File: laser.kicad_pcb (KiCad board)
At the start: 2 copper layers, 90.2 x 50.9 mm, 127 parts, among them IC201 ADM7172ACPZ-4.2-R7, IC202 LT1716CS5#TRPBF, IC203 ADM7154ARDZ-3.3-R7, IC204 IRF9358PBF, IC601 ATMEGA328P-AU, IC602 FT232RL-TUBE, IC701 MAX6126AASA25+, IC801 ADS122C04IPWR, J601 M20-9980345, J602 USB_Connector, Q401 RSR030N06TL, U101 281698-3, U201 LM4040EIM3X-2.5_NOPB, U301 OPA569AIDWPR, U302 OPA569AIDWPR, U401 ADA4528-2ACPZ-RL, U402 782853152_WE-CBA_08, U501 ADA4528-2ACPZ-RL, U502 ADA4528-2ACPZ-RL, U801 MAX5217GUA+, U802 MAX5217GUA+, Y601 ECS-160-16-33B-CKM-TR

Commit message: SOLVED: GND and 4.2V
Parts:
- moved C606 11.9 mm to (199.7, 101.5), turned to 90 degrees
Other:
- copper layers 2 -> 4
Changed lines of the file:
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@@
   (layers
     (0 F.Cu signal)
+    (1 GND power)
+    (2 PWR power)
     (31 B.Cu signal)
     (32 B.Adhes user)
@@
   )
   (module Capacitor_SMD:C_0402_1005Metric (layer F.Cu)
-    (at 200.09 89.61)
-    (descr "Capacitor SMD 0402 (1005 Metric), square (rectangular) end terminal, IPC_7351 nominal, (Body size source: IPC-SM-782 page 76, https://www.pcb-3d.com/wordpress/wp-content/uploads/ipc-sm-782a_amendment_1_and_2.pdf), generated with kicad-footprint-generator")
-    (tags capacitor)
-    (attr smd)
-    (fp_text reference C606 (at 0 -1.16) (layer F.SilkS)
-      (effects (font (size 1 1) (thickness 0.15)))
-    )
-    (fp_text value 100nF (at 0 1.16) (layer F.Fab)
-      (effects (font (size 1 1) (thickness 0.15)))
-    )
-    (fp_line (start -0.5 0.25) (end -0.5 -0.25) (layer F.Fab) (width 0.1))
-    (fp_line (start -0.5 -0.25) (end 0.5 -0.25) (layer F.Fab) (width 0.1))
-    (fp_line (start 0.5 -0.25) (end 0.5 0.25) (layer F.Fab) (width 0.1))
-    (fp_line (start 0.5 0.25) (end -0.5 0.25) (layer F.Fab) (width 0.1))
-    (fp_line (start -0.107836 -0.36) (end 0.107836 -0.36) (layer F.SilkS) (width 0.12))
-    (fp_line (start -0.107836 0.36) (end 0.107836 0.36) (layer F.SilkS) (width 0.12))
-    (fp_line (start -0.91 0.46) (end -0.91 -0.46) (layer F.CrtYd) (width 0.05))
-    (fp_line (start -0.91 -0.46) (end 0.91 -0.46) (layer F.CrtYd) (width 0.05))
-    (fp_line (start 0.91 -0.46) (end 0.91 0.46) (layer F.CrtYd) (width 0.05))
-    (fp_line (start 0.91 0.46) (end -0.91 0.46) (layer F.CrtYd) (width 0.05))
-    (fp_text user %R (at 0 0) (layer F.Fab)
-      (effects (font (size 0.25 0.25) (thickness 0.04)))
-    )
-    (pad 1 smd roundrect (at -0.48 0) (size 0.56 0.62) (layers F.Cu F.Paste F.Mask) (roundrect_rratio 0.25)
+    (at 199.73 101.53 90)
+    (descr "Capacitor SMD 0402 (1005 Metric), square (rectangular) end terminal, IPC_7351 nominal, (Body size source: IPC-SM-782 page 76, https://www.pcb-3d.com/wordpress/wp-content/uploads/ipc-sm-782a_amendment_1_and_2.pdf), generated with kicad-footprint-generator")
+    (tags capacitor)
+    (attr smd)
+    (fp_text reference C606 (at 0 -1.16 90) (layer F.SilkS)
+      (effects (font (size 1 1) (thickness 0.15)))
+    )
+    (fp_text value 100nF (at 0 1.16 90) (layer F.Fab)
+      (effects (font (size 1 1) (thickness 0.15)))
+    )
+    (fp_line (start -0.5 0.25) (end -0.5 -0.25) (layer F.Fab) (width 0.1))
+    (fp_line (start -0.5 -0.25) (end 0.5 -0.25) (layer F.Fab) (width 0.1))
+    (fp_line (start 0.5 -0.25) (end 0.5 0.25) (layer F.Fab) (width 0.1))
+    (fp_line (start 0.5 0.25) (end -0.5 0.25) (layer F.Fab) (width 0.1))
+    (fp_line (start -0.107836 -0.36) (end 0.107836 -0.36) (layer F.SilkS) (width 0.12))
+    (fp_line (start -0.107836 0.36) (end 0.107836 0.36) (layer F.SilkS) (width 0.12))
+    (fp_line (start -0.91 0.46) (end -0.91 -0.46) (layer F.CrtYd) (width 0.05))
+    (fp_line (start -0.91 -0.46) (end 0.91 -0.46) (layer F.CrtYd) (width 0.05))
+    (fp_line (start 0.91 -0.46) (end 0.91 0.46) (layer F.CrtYd) (width 0.05))
+    (fp_line (start 0.91 0.46) (end -0.91 0.46) (layer F.CrtYd) (width 0.05))
+    (fp_text user %R (at 0 0 90) (layer F.Fab)
+      (effects (font (size 0.25 0.25) (thickness 0.04)))
+    )
+    (pad 1 smd roundrect (at -0.48 0 90) (size 0.56 0.62) (layers F.Cu F.Paste F.Mask) (roundrect_rratio 0.25)
       (net 35 "Net-(C606-Pad1)"))
-    (pad 2 smd roundrect (at 0.48 0) (size 0.56 0.62) (layers F.Cu F.Paste F.Mask) (roundrect_rratio 0.25)
-      (net 2 4.2V))
-    (model ${KISYS3DMOD}/Capacitor_SMD.3dshapes/C_0402_1005Metric.wrl
+    (pad 2 smd roundrect (at 0.48 0 90) (size 0.56 0.62) (layers F.Cu F.Paste F.Mask) (roundrect_rratio 0.25)
+      (net 2 4.2V))
+    (model ${KISYS3DMOD}/Capacitor_SMD.3dshapes/C_0402_1005Metric.wrl

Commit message: final push for any last changes 6/18
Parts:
- added C305: 100u, Capacitor_SMD:C_0402_1005Metric, F.Cu at (165.8, 118.4)
- added C306: 100u, Capacitor_SMD:C_0402_1005Metric, F.Cu at (166.3, 123.2)
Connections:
- B1 pad 2: 4.2V -> Monitor+_To_AIN2
- B1 pad 4: 4.2V -> Monitor+_To_AIN2
- B1 pad 5: 4.2V -> Monitor+_To_AIN2
- B1 pad 8: 4.2V -> Monitor+_To_AIN2
- B1 pad 9: 4.2V -> Monitor+_To_AIN2
- C201 pad 2: 4.2V -> Monitor+_To_AIN2
- C202 pad 2: 4.2V -> Monitor+_To_AIN2
- C203 pad 2: 4.2V -> Monitor+_To_AIN2
- C204 pad 1: 4.2V -> Monitor+_To_AIN2
- C206 pad 1: 4.2V -> Monitor+_To_AIN2
- C207 pad 1: 4.2V -> Monitor+_To_AIN2
- C208 pad 1: 4.2V -> Monitor+_To_AIN2
- C209 pad 2: 4.2V -> Monitor+_To_AIN2
- C210 pad 1: 4.2V -> Monitor+_To_AIN2
- C211 pad 1: 4.2V -> Monitor+_To_AIN2
- C212 pad 2: 4.2V -> Monitor+_To_AIN2
- C302 pad 1: 4.2V -> Monitor+_To_AIN2
- C303 pad 1: 4.2V -> Monitor+_To_AIN2
- C307 pad 2: 4.2V -> Monitor+_To_AIN2
- C308 pad 2: 4.2V -> Monitor+_To_AIN2
- C309 pad 1: 4.2V -> Monitor+_To_AIN2
- C310 pad 1: 4.2V -> Monitor+_To_AIN2
- C311 pad 1: 4.2V -> Monitor+_To_AIN2
- C312 pad 1: 4.2V -> Monitor+_To_AIN2
- C402 pad 1: 4.2V -> Monitor+_To_AIN2
- C403 pad 2: 4.2V -> Monitor+_To_AIN2
- C404 pad 2: 4.2V -> Monitor+_To_AIN2
- C405 pad 2: 4.2V -> Monitor+_To_AIN2
- C406 pad 2: 4.2V -> Monitor+_To_AIN2
- C407 pad 1: 4.2V -> Monitor+_To_AIN2
- C408 pad 2: 4.2V -> Monitor+_To_AIN2
- C501 pad 2: 4.2V -> Monitor+_To_AIN2
- C502 pad 2: 4.2V -> Monitor+_To_AIN2
- C503 pad 2: 4.2V -> Monitor+_To_AIN2
- C504 pad 2: 4.2V -> Monitor+_To_AIN2
- C505 pad 2: 4.2V -> Monitor+_To_AIN2
- C506 pad 2: 4.2V -> Monitor+_To_AIN2
- C507 pad 2: 4.2V -> Monitor+_To_AIN2
- C601 pad 2: 4.2V -> Monitor+_To_AIN2
- C602 pad 2: 4.2V -> Monitor+_To_AIN2
- C603 pad 2: 4.2V -> Monitor+_To_AIN2
- C604 pad 2: 4.2V -> Monitor+_To_AIN2
- C605 pad 2: 4.2V -> Monitor+_To_AIN2
- C606 pad 2: 4.2V -> Monitor+_To_AIN2
- C701 pad 2: 4.2V -> Monitor+_To_AIN2
- C702 pad 2: 4.2V -> Monitor+_To_AIN2
- C703 pad 2: 4.2V -> Monitor+_To_AIN2
- C704 pad 2: 4.2V -> Monitor+_To_AIN2
- C705 pad 2: 4.2V -> Monitor+_To_AIN2
- C801 pad 2: 4.2V -> Monitor+_To_AIN2
- C802 pad 2: 4.2V -> Monitor+_To_AIN2
- C803 pad 2: 4.2V -> Monitor+_To_AIN2
- C804 pad 2: 4.2V -> Monitor+_To_AIN2
- C805 pad 2: 4.2V -> Monitor+_To_AIN2
- C806 pad 2: 4.2V -> Monitor+_To_AIN2
- C807 pad 2: 4.2V -> Monitor+_To_AIN2
- C808 pad 2: 4.2V -> Monitor+_To_AIN2
- C809 pad 2: 4.2V -> Monitor+_To_AIN2
- C810 pad 2: 4.2V -> Monitor+_To_AIN2
- C811 pad 2: 4.2V -> Monitor+_To_AIN2
- IC201 pad 6: 4.2V -> Monitor+_To_AIN2
- IC201 pad 9: 4.2V -> Monitor+_To_AIN2
- IC202 pad 2: 4.2V -> Monitor+_To_AIN2
- IC203 pad 4: 4.2V -> Monitor+_To_AIN2
- IC204 pad 2: 4.2V -> Monitor+_To_AIN2
- IC601 pad 21: 4.2V -> Monitor+_To_AIN2
- IC601 pad 3: 4.2V -> Monitor+_To_AIN2
- IC601 pad 5: 4.2V -> Monitor+_To_AIN2
- IC602 pad 18: 4.2V -> Monitor+_To_AIN2
- IC602 pad 21: 4.2V -> Monitor+_To_AIN2
- IC602 pad 25: 4.2V -> Monitor+_To_AIN2
- IC602 pad 26: 4.2V -> Monitor+_To_AIN2
- IC602 pad 7: 4.2V -> Monitor+_To_AIN2
- IC701 pad 3: 4.2V -> Monitor+_To_AIN2
- IC701 pad 4: 4.2V -> Monitor+_To_AIN2
- IC801 pad 1: 4.2V -> Monitor+_To_AIN2
- IC801 pad 10: 4.2V -> Monitor+_To_AIN2
- IC801 pad 2: 4.2V -> Monitor+_To_AIN2
- IC801 pad 4: 4.2V -> Monitor+_To_AIN2
- IC801 pad 5: 4.2V -> Monitor+_To_AIN2
- IC801 pad 7: 4.2V -> Monitor+_To_AIN2
- IC801 pad 8: 4.2V -> Monitor+_To_AIN2
- J601 pad 6: 4.2V -> Monitor+_To_AIN2
- J602 pad 1: 4.2V -> Monitor+_To_AIN2
- J602 pad 6: 4.2V -> Monitor+_To_AIN2
- J602 pad 7: 4.2V -> Monitor+_To_AIN2
- J602 pad 8: 4.2V -> Monitor+_To_AIN2
- J602 pad 9: 4.2V -> Monitor+_To_AIN2
- R203 pad 2: 4.2V -> Monitor+_To_AIN2
- R302 pad 2: 4.2V -> Monitor+_To_AIN2
- R305 pad 2: 4.2V -> Monitor+_To_AIN2
- R306 pad 2: 4.2V -> Monitor+_To_AIN2
- R308 pad 1: 4.2V -> Monitor+_To_AIN2
- R309 pad 1: 4.2V -> Monitor+_To_AIN2
- R407 pad E1: 4.2V -> Monitor+_To_AIN2
- R407 pad I1: 4.2V -> Monitor+_To_AIN2
- R803 pad 2: 4.2V -> Monitor+_To_AIN2
- R804 pad 2: 4.2V -> Monitor+_To_AIN2
- U101 pad 1: 4.2V -> Monitor+_To_AIN2
- U201 pad 2: 4.2V -> Monitor+_To_AIN2
- U301 pad 1: 4.2V -> Monitor+_To_AIN2
- U301 pad 10: 4.2V -> Monitor+_To_AIN2
- U301 pad 11: 4.2V -> Monitor+_To_AIN2
- U301 pad 13: Net-(C305-Pad2) -> 4.2V
- U301 pad 17: 4.2V -> Monitor+_To_AIN2
- U301 pad 18: 4.2V -> Monitor+_To_AIN2
- U301 pad 20: 4.2V -> Monitor+_To_AIN2
- U302 pad 1: 4.2V -> Monitor+_To_AIN2
- U302 pad 10: 4.2V -> Monitor+_To_AIN2
- U302 pad 11: 4.2V -> Monitor+_To_AIN2
- U302 pad 13: Net-(C306-Pad2) -> 4.2V
- U302 pad 17: 4.2V -> Monitor+_To_AIN2
- U302 pad 18: 4.2V -> Monitor+_To_AIN2
- U302 pad 20: 4.2V -> Monitor+_To_AIN2
- U401 pad 4: 4.2V -> Monitor+_To_AIN2
- U501 pad 4: 4.2V -> Monitor+_To_AIN2
- U502 pad 4: 4.2V -> Monitor+_To_AIN2
- U801 pad 8: 4.2V -> Monitor+_To_AIN2
- U802 pad 2: 4.2V -> Monitor+_To_AIN2
- U802 pad 8: 4.2V -> Monitor+_To_AIN2
- Y601 pad 2: 4.2V -> Monitor+_To_AIN2
- Y601 pad 4: 4.2V -> Monitor+_To_AIN2

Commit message: GND works
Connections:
- B1 pad 2: Monitor+_To_AIN2 -> GND
- B1 pad 5: Monitor+_To_AIN2 -> GND
- B1 pad 8: Monitor+_To_AIN2 -> GND
- B1 pad 9: Monitor+_To_AIN2 -> GND
- C201 pad 2: Monitor+_To_AIN2 -> GND
- C202 pad 2: Monitor+_To_AIN2 -> GND
- C203 pad 2: Monitor+_To_AIN2 -> GND
- C204 pad 1: Monitor+_To_AIN2 -> GND
- C206 pad 1: Monitor+_To_AIN2 -> GND
- C207 pad 1: Monitor+_To_AIN2 -> GND
- C208 pad 1: Monitor+_To_AIN2 -> GND
- C209 pad 2: Monitor+_To_AIN2 -> GND
- C210 pad 1: Monitor+_To_AIN2 -> GND
- C211 pad 1: Monitor+_To_AIN2 -> GND
- C212 pad 2: Monitor+_To_AIN2 -> GND
- C302 pad 1: Monitor+_To_AIN2 -> GND
- C303 pad 1: Monitor+_To_AIN2 -> GND
- C305 pad 1: Monitor+_To_AIN2 -> GND
- C306 pad 1: Monitor+_To_AIN2 -> GND
- C307 pad 2: Monitor+_To_AIN2 -> GND
- C308 pad 2: Monitor+_To_AIN2 -> GND
- C309 pad 1: Monitor+_To_AIN2 -> GND
- C310 pad 1: Monitor+_To_AIN2 -> GND
- C311 pad 1: Monitor+_To_AIN2 -> GND
- C312 pad 1: Monitor+_To_AIN2 -> GND
- C402 pad 1: Monitor+_To_AIN2 -> GND
- C403 pad 2: Monitor+_To_AIN2 -> GND
- C404 pad 2: Monitor+_To_AIN2 -> GND
- C405 pad 2: Monitor+_To_AIN2 -> GND
- C406 pad 2: Monitor+_To_AIN2 -> GND
- C407 pad 1: Monitor+_To_AIN2 -> GND
- C408 pad 2: Monitor+_To_AIN2 -> GND
- C501 pad 2: Monitor+_To_AIN2 -> GND
- C502 pad 2: Monitor+_To_AIN2 -> GND
- C503 pad 2: Monitor+_To_AIN2 -> GND
- C504 pad 2: Monitor+_To_AIN2 -> GND
- C505 pad 2: Monitor+_To_AIN2 -> GND
- C506 pad 2: Monitor+_To_AIN2 -> GND
- C507 pad 2: Monitor+_To_AIN2 -> GND
- C601 pad 2: Monitor+_To_AIN2 -> GND
- C602 pad 2: Monitor+_To_AIN2 -> GND
- C603 pad 2: Monitor+_To_AIN2 -> GND
- C604 pad 2: Monitor+_To_AIN2 -> GND
- C605 pad 2: Monitor+_To_AIN2 -> GND
- C606 pad 2: Monitor+_To_AIN2 -> GND
- C701 pad 2: Monitor+_To_AIN2 -> GND
- C702 pad 2: Monitor+_To_AIN2 -> GND
- C703 pad 2: Monitor+_To_AIN2 -> GND
- C704 pad 2: Monitor+_To_AIN2 -> GND
- C705 pad 2: Monitor+_To_AIN2 -> GND
- C801 pad 2: Monitor+_To_AIN2 -> GND
- C802 pad 2: Monitor+_To_AIN2 -> GND
- C803 pad 2: Monitor+_To_AIN2 -> GND
- C804 pad 2: Monitor+_To_AIN2 -> GND
- C805 pad 2: Monitor+_To_AIN2 -> GND
- C806 pad 2: Monitor+_To_AIN2 -> GND
- C807 pad 2: Monitor+_To_AIN2 -> GND
- C808 pad 2: Monitor+_To_AIN2 -> GND
- C809 pad 2: Monitor+_To_AIN2 -> GND
- C810 pad 2: Monitor+_To_AIN2 -> GND
- C811 pad 2: Monitor+_To_AIN2 -> GND
- IC201 pad 6: Monitor+_To_AIN2 -> GND
- IC201 pad 9: Monitor+_To_AIN2 -> GND
- IC202 pad 2: Monitor+_To_AIN2 -> GND
- IC203 pad 4: Monitor+_To_AIN2 -> GND
- IC204 pad 2: Monitor+_To_AIN2 -> GND
- IC601 pad 21: Monitor+_To_AIN2 -> GND
- IC601 pad 3: Monitor+_To_AIN2 -> GND
- IC601 pad 5: Monitor+_To_AIN2 -> GND
- IC602 pad 18: Monitor+_To_AIN2 -> GND
- IC602 pad 21: Monitor+_To_AIN2 -> GND
- IC602 pad 25: Monitor+_To_AIN2 -> GND
- IC602 pad 26: Monitor+_To_AIN2 -> GND
- IC602 pad 7: Monitor+_To_AIN2 -> GND
- IC701 pad 3: Monitor+_To_AIN2 -> GND
- IC701 pad 4: Monitor+_To_AIN2 -> GND
- IC801 pad 1: Monitor+_To_AIN2 -> GND
- IC801 pad 10: Monitor+_To_AIN2 -> GND
- IC801 pad 2: Monitor+_To_AIN2 -> GND
- IC801 pad 4: Monitor+_To_AIN2 -> GND
- IC801 pad 5: Monitor+_To_AIN2 -> GND
- IC801 pad 8: Monitor+_To_AIN2 -> GND
- J601 pad 6: Monitor+_To_AIN2 -> GND
- J602 pad 1: Monitor+_To_AIN2 -> GND
- J602 pad 6: Monitor+_To_AIN2 -> GND
- J602 pad 7: Monitor+_To_AIN2 -> GND
- J602 pad 8: Monitor+_To_AIN2 -> GND
- J602 pad 9: Monitor+_To_AIN2 -> GND
- R203 pad 2: Monitor+_To_AIN2 -> GND
- R302 pad 2: Monitor+_To_AIN2 -> GND
- R305 pad 2: Monitor+_To_AIN2 -> GND
- R306 pad 2: Monitor+_To_AIN2 -> GND
- R308 pad 1: Monitor+_To_AIN2 -> GND
- R309 pad 1: Monitor+_To_AIN2 -> GND
- R407 pad E1: Monitor+_To_AIN2 -> GND
- R407 pad I1: Monitor+_To_AIN2 -> GND
- R803 pad 2: Monitor+_To_AIN2 -> GND
- R804 pad 2: Monitor+_To_AIN2 -> GND
- U101 pad 1: Monitor+_To_AIN2 -> GND
- U201 pad 2: Monitor+_To_AIN2 -> GND
- U301 pad 1: Monitor+_To_AIN2 -> GND
- U301 pad 10: Monitor+_To_AIN2 -> GND
- U301 pad 11: Monitor+_To_AIN2 -> GND
- U301 pad 17: Monitor+_To_AIN2 -> GND
- U301 pad 18: Monitor+_To_AIN2 -> GND
- U301 pad 20: Monitor+_To_AIN2 -> GND
- U302 pad 1: Monitor+_To_AIN2 -> GND
- U302 pad 10: Monitor+_To_AIN2 -> GND
- U302 pad 11: Monitor+_To_AIN2 -> GND
- U302 pad 17: Monitor+_To_AIN2 -> GND
- U302 pad 18: Monitor+_To_AIN2 -> GND
- U302 pad 20: Monitor+_To_AIN2 -> GND
- U401 pad 4: Monitor+_To_AIN2 -> GND
- U501 pad 4: Monitor+_To_AIN2 -> GND
- U502 pad 4: Monitor+_To_AIN2 -> GND
- U801 pad 8: Monitor+_To_AIN2 -> GND
- U802 pad 2: Monitor+_To_AIN2 -> GND
- U802 pad 8: Monitor+_To_AIN2 -> GND
- Y601 pad 2: Monitor+_To_AIN2 -> GND
- Y601 pad 4: Monitor+_To_AIN2 -> GND

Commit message: trying to figure out how to connect gnd to plane
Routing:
- net GND: track 0.00 -> 8.93 mm
- added copper zone on GND, net GND
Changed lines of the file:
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@@
     (thickness 1.6)
     (drawings 17)
-    (tracks 8)
+    (tracks 10)
     (zones 0)
     (modules 129)
@@
   (layers
     (0 F.Cu signal)
-    (1 GND power)
+    (1 GND power hide)
     (2 PWR power)
     (31 B.Cu signal)
@@
   (via (at 205.867 83.9038) (size 2.4892) (layers F.Cu B.Cu) (net 0))
   (via (at 152.2984 121.2672) (size 2.4892) (layers F.Cu B.Cu) (net 0))
+  (segment (start 210.17 114.11) (end 207.5 116.78) (width 0.25) (layer F.Cu) (net 126))
+  (segment (start 210.17 108.96) (end 210.17 114.11) (width 0.25) (layer F.Cu) (net 126))
+  (zone (net 126) (net_name GND) (layer GND) (hatch edge 0.508)
+    (connect_pads (clearance 0.508))
+    (min_thickness 0.254)
+    (fill yes (arc_segments 32) (thermal_gap 0.508) (thermal_bridge_width 0.508))
+    (polygon
+      (pts
+        (xy 208.2 81.13) (xy 208.2 87.11) (xy 213.25 87.08) (xy 213.22 126.44) (xy 208.2 126.46)
+        (xy 208.23 132.46) (xy 127.34 132.51) (xy 127.46 126.52) (xy 122.51 126.52) (xy 122.56 115.48)
+        (xy 155.56 115.42) (xy 155.56 97.99) (xy 122.54 98.02) (xy 122.59 87.07) (xy 127.53 87.05)
+        (xy 127.55 81.06)
+      )
+    )
+  )
 )

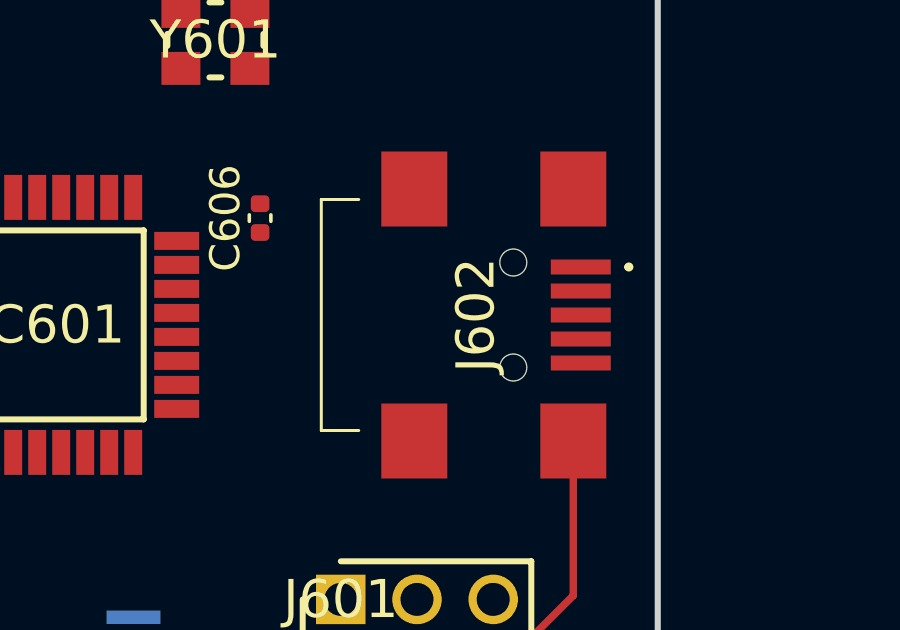
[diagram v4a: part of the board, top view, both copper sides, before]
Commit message: connect ground
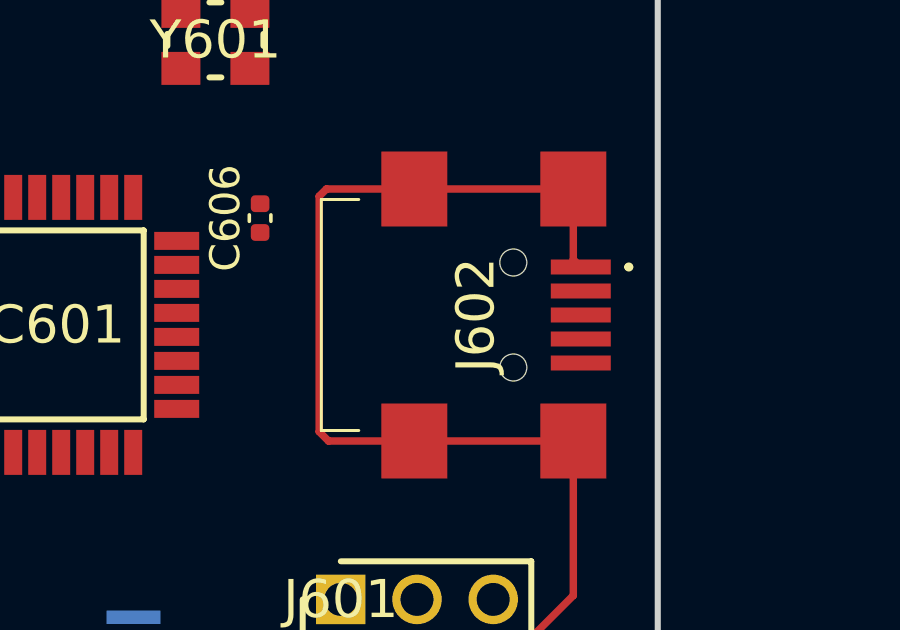
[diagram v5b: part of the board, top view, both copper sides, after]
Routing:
- net GND: track 8.93 -> 36.6 mm

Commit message: finished initial layout
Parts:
- C403, C404, C701, L201: moved to B.Cu
- moved C801 140.8 mm to (199.3, 148.8)
- moved C804 140.8 mm to (199.3, 150.8)
- moved R801 140.8 mm to (195.1, 146.8)
- moved R802 140.8 mm to (202.4, 142.2)
- moved R807 140.8 mm to (202.4, 144.2)
- moved C803 140.8 mm to (205.3, 144.1)
- moved C807 140.8 mm to (203.8, 146.2)
- moved C809 140.8 mm to (205.3, 142.2)
- moved C810 140.8 mm to (205.0, 148.1)
- moved R803 140.8 mm to (193.5, 150.9)
- moved R804 140.8 mm to (196.4, 148.8)
- moved R805 140.8 mm to (198.0, 146.8)
- moved R806 140.8 mm to (193.5, 149.0)
- moved C802 140.8 mm to (200.9, 146.8)
- moved C805 140.8 mm to (202.2, 148.8)
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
